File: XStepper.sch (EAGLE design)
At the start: 75 parts, among them IC2 7812TV, Q2 16 MHZ

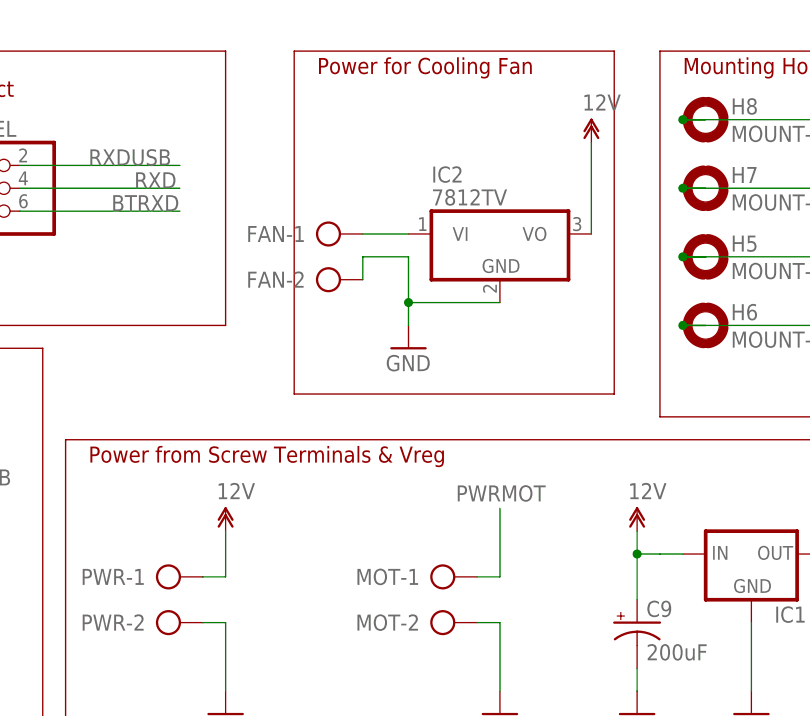
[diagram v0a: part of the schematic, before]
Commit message: - add 7812 regulator for fan and main 5V voltage regulator
- change c10 to small cap cuz he get only 12v with new regulator
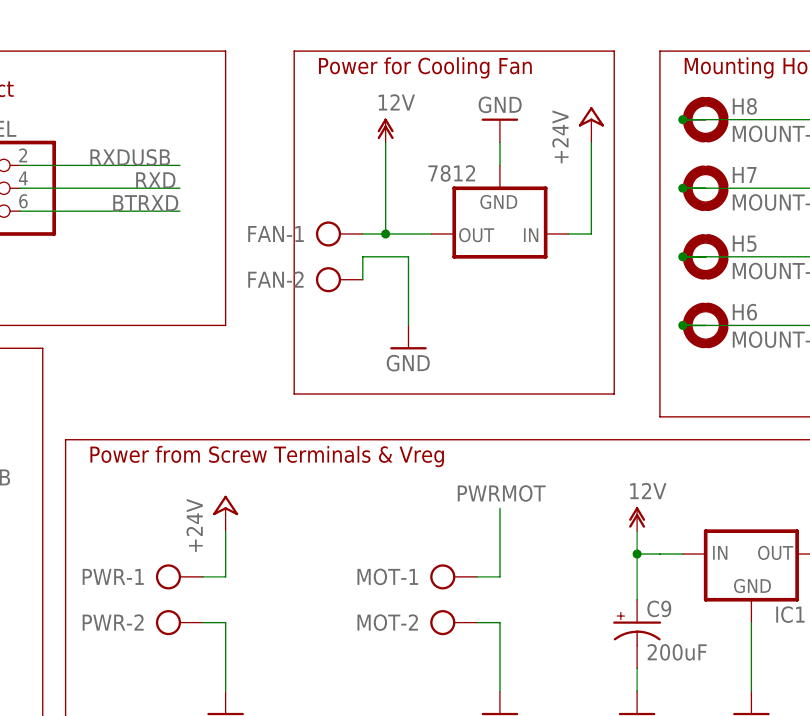
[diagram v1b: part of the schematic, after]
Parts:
- removed IC2: 7812TV, linear:7812TV
- added 7812: (no value), SparkFun-PowerIC:V_REG_78XXSINK
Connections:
- removed net N$46: FAN-1.KL, IC2.VI
- new net +24V: 7812.IN, PWR-1.KL
- net 12V: now also 7812.OUT, FAN-1.KL; no longer IC2.VO, PWR-1.KL
- net GND: now also 7812.GND; no longer IC2.GND
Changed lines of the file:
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@@
 <part name="GND13" library="SparkFun" deviceset="GND" device=""/>
 <part name="GND25" library="SparkFun" deviceset="GND" device=""/>
-<part name="U$33" library="12v" deviceset="12V" device=""/>
 <part name="GND14" library="SparkFun" deviceset="GND" device=""/>
 <part name="GND22" library="SparkFun" deviceset="GND" device=""/>
@@
 <part name="GND21" library="SparkFun" deviceset="GND" device=""/>
 <part name="D2" library="SparkFun-DiscreteSemi" deviceset="DIODE" device="PTH"/>
-<part name="IC2" library="linear" deviceset="78*" device="TV" technology="12"/>
+<part name="7812" library="SparkFun-PowerIC" deviceset="V_REG_78XX" device="SINK"/>
+<part name="GND27" library="SparkFun" deviceset="GND" device=""/>
+<part name="P+1" library="supply1" deviceset="+24V" device=""/>
+<part name="P+2" library="supply1" deviceset="+24V" device=""/>
 <part name="U$2" library="12v" deviceset="12V" device=""/>
 </parts>
@@
 <instance part="GND13" gate="1" x="177.8" y="106.68"/>
 <instance part="GND25" gate="1" x="132.08" y="106.68"/>
-<instance part="U$33" gate="G$1" x="132.08" y="127"/>
 <instance part="GND14" gate="1" x="203.2" y="106.68"/>
 <instance part="GND22" gate="1" x="190.5" y="106.68"/>
@@
 <instance part="GND21" gate="1" x="30.48" y="124.46" rot="R90"/>
 <instance part="D2" gate="G$1" x="236.22" y="165.1"/>
-<instance part="IC2" gate="A1" x="162.56" y="160.02"/>
-<instance part="U$2" gate="G$1" x="172.72" y="170.18"/>
+<instance part="7812" gate="G$1" x="162.56" y="160.02" rot="R180"/>
+<instance part="GND27" gate="1" x="162.56" y="172.72" rot="R180"/>
+<instance part="P+1" gate="1" x="132.08" y="129.54"/>
+<instance part="P+2" gate="1" x="172.72" y="172.72"/>
+<instance part="U$2" gate="G$1" x="149.86" y="170.18"/>
 </instances>
 <busses>
@@
 </segment>
 <segment>
-<wire x1="152.4" y1="149.86" x2="152.4" y2="152.4" width="0.1524" layer="91"/>
 <pinref part="GND18" gate="1" pin="GND"/>
 <pinref part="FAN" gate="-2" pin="KL"/>
-<wire x1="152.4" y1="152.4" x2="152.4" y2="157.48" width="0.1524" layer="91"/>
+<wire x1="152.4" y1="149.86" x2="152.4" y2="157.48" width="0.1524" layer="91"/>
 <wire x1="147.32" y1="154.94" x2="147.32" y2="157.48" width="0.1524" layer="91"/>
 <wire x1="147.32" y1="157.48" x2="152.4" y2="157.48" width="0.1524" layer="91"/>
-<pinref part="IC2" gate="A1" pin="GND"/>
-<wire x1="162.56" y1="152.4" x2="152.4" y2="152.4" width="0.1524" layer="91"/>
-<junction x="152.4" y="152.4"/>
 </segment>
 <segment>
@@
 <wire x1="25.4" y1="124.46" x2="27.94" y2="124.46" width="0.1524" layer="91"/>
 </segment>
+<segment>
+<pinref part="7812" gate="G$1" pin="GND"/>
+<wire x1="162.56" y1="167.64" x2="162.56" y2="170.18" width="0.1524" layer="91"/>
+<pinref part="GND27" gate="1" pin="GND"/>
+</segment>
 </net>
 <net name="N$5" class="0">
@@
 </segment>
 <segment>
-<pinref part="PWR" gate="-1" pin="KL"/>
-<pinref part="U$33" gate="G$1" pin="12V"/>
-<wire x1="129.54" y1="121.92" x2="132.08" y2="121.92" width="0.1524" layer="91"/>
-<wire x1="132.08" y1="121.92" x2="132.08" y2="127" width="0.1524" layer="91"/>
-</segment>
-<segment>
-<pinref part="IC2" gate="A1" pin="VO"/>
-<wire x1="172.72" y1="160.02" x2="172.72" y2="170.18" width="0.1524" layer="91"/>
+<pinref part="7812" gate="G$1" pin="OUT"/>
+<pinref part="FAN" gate="-1" pin="KL"/>
+<wire x1="154.94" y1="160.02" x2="149.86" y2="160.02" width="0.1524" layer="91"/>
 <pinref part="U$2" gate="G$1" pin="12V"/>
+<wire x1="149.86" y1="160.02" x2="147.32" y2="160.02" width="0.1524" layer="91"/>
+<wire x1="149.86" y1="170.18" x2="149.86" y2="160.02" width="0.1524" layer="91"/>
+<junction x="149.86" y="160.02"/>
 </segment>
 </net>
@@
 </segment>
 </net>
-<net name="N$46" class="1">
-<segment>
-<pinref part="FAN" gate="-1" pin="KL"/>
-<pinref part="IC2" gate="A1" pin="VI"/>
-<wire x1="147.32" y1="160.02" x2="152.4" y2="160.02" width="0.1524" layer="91"/>
-</segment>
-</net>
+<net name="+24V" class="1">
+<segment>
+<pinref part="PWR" gate="-1" pin="KL"/>
+<wire x1="129.54" y1="121.92" x2="132.08" y2="121.92" width="0.1524" layer="91"/>
+<wire x1="132.08" y1="121.92" x2="132.08" y2="127" width="0.1524" layer="91"/>
+<pinref part="P+1" gate="1" pin="+24V"/>
+</segment>
+<segment>
+<pinref part="7812" gate="G$1" pin="IN"/>
+<wire x1="170.18" y1="160.02" x2="172.72" y2="160.02" width="0.1524" layer="91"/>
+<wire x1="172.72" y1="160.02" x2="172.72" y2="170.18" width="0.1524" layer="91"/>
+<pinref part="P+2" gate="1" pin="+24V"/>
+</segment>
+</net>

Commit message: - last design from matt
- correct some issues
- run all eagle tests
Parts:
- removed 7812: (no value), SparkFun-PowerIC:V_REG_78XXSINK
- removed ALED, PWRLED1, XLED, XSTLED, YLED, YSTLED, ZLED, ZSTLED: (no value), led:LED3MM
- removed COMMSEL: (no value), pinhead:PINHD-2X3
- removed D2: (no value), SparkFun-DiscreteSemi:DIODEPTH
- removed ESTOP>, MOT: (no value), con-ptr500:AK500/2
- removed GND: (no value), jumper:JP1E
- removed OK1, OK2: 6N137, optocoupler:6N137
- added AD, XD, YD, ZD: green, SparkFun-LED:LED3MM
- added C16: 0.1uF, resistor:C-EU025-025X050
- added C17, C19: 0.1uF, SparkFun-Capacitors:CAP1206
- added C20: 10uF, SparkFun-Capacitors:CAP_POL1206
- added C21: 200uF, resistor:CPOL-USE3.5-8
- added D1: (no value), SparkFun-DiscreteSemi:DIODEPTH
- added DIR: DIR, SparkFun-Passives:SOLDERJUMPER_2WAYW
- added EN: EN, SparkFun-Passives:SOLDERJUMPER_2WAYW
- added ESTOP, VMOT: (no value), con-ptr500:AK500/2
- added IC2: L7812, SparkFun-PowerIC:V_REG_78XXSINK
- added JP2, JP3, JP4: (no value), SparkFun-Connectors:M04PTH
- added JP5, JP6: (no value), SparkFun-Connectors:M03X2POGO_PINS
- added JP7: USBSMD, SparkFun-Connectors:USBSMD
- added JP8: USB-B, SparkFun-Connectors:USBPTH
- added OK3: HCPL2630, optocoupler:HCPL2630
- added R15, R16: 110, SparkFun-Resistors:RESISTORAXIAL-0.3
- added R22, R23: 470, SparkFun-Resistors:RESISTORAXIAL-0.3
- added RX: Grn, SparkFun-LED:LED1206
- added S1: (no value), SparkFun-Electromechanical:TAC_SWITCHSMD
- added SJ4: NO, SparkFun-Passives:SOLDERJUMPERNO
- added TX: Red, SparkFun-LED:LED1206
- added U1: FT232RL-BASICSSOP, SparkFun-DigitalIC:FT232RL-BASICSSOP
- added VCC: orange, SparkFun-LED:LED3MM
- added X, Y, Z: red, SparkFun-LED:LED3MM
- A-AXIS, X-AXIS, Y-AXIS, Z-AXIS: value (none) -> 2x03
- C10: value 100uF -> 47uF
- C9: value 200uF -> 100uF
- IC1: value (none) -> L7805
- JP1: device pinhead:PINHD-2X3 -> SparkFun-Connectors:M04PTH
- R10, R11: value 470 -> 220
- R13, R14: value 220 -> 10K; device SparkFun-Resistors:RESISTORAXIAL-0.3 -> SparkFun-Resistors:RESISTOR1206
- R3: device SparkFun-Resistors:RESISTORPTH-1/6W -> SparkFun-Resistors:RESISTORAXIAL-0.3
- R6, R7: value 110 -> 330
- R8, R9: value 470 -> 1K; device SparkFun-Resistors:RESISTORAXIAL-0.3 -> SparkFun-Resistors:RESISTOR1206
- XLIM, YLIM, ZLIM: device pinhead:PINHD-1X3 -> SparkFun-Connectors:M03POLAR
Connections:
- net MOTOR_DISABLE renamed ENABLE
- removed net +24V: 7812.IN, PWR-1.KL
- removed net 12V: 7812.OUT, C9.+, FAN-1.KL, IC1.IN
- removed net BTRXD: BT-TTL.3, COMMSEL.6
- removed net BTTXD: BT-TTL.4, COMMSEL.5
- removed net N$10: STEPPERDRIVER1.MOT-1A, YMOT-2.KL
- removed net N$27: AMOT-3.KL, STEPPERDRIVER3.MOT-2A
- removed net N$38: R4.1, XLED.A
- removed net N$39: R5.1, YLED.A
- removed net N$40: R6.1, ZLED.A
- removed net N$41: ALED.A, R7.1
- removed net N$42: R13.2, YSTLED.A
- removed net N$44: R14.2, ZSTLED.A
- removed net PWRMOT: C2.+, C4.+, C6.+, C8.+, MOT-1.KL, STEPPERDRIVER.VMOT, STEPPERDRIVER1.VMOT, STEPPERDRIVER2.VMOT, STEPPERDRIVER3.VMOT
- removed net RXD: 328P.PD0(RXD), COMMSEL.4
- removed net RXDUSB: COMMSEL.2, OK2.VO, R9.2
- removed net TXD: 328P.PD1(TXD), COMMSEL.3
- removed net TXDUSB: COMMSEL.1, R11.2
- removed net USB_5V: C11.1, OK1.VCC, OK1.VE, OK2.A, R10.2, TTL.3
- removed net USB_GND: C11.2, GND.1, OK1.GND, TTL.1, TTL.2
- removed net USB_RXD: OK1.VO, R10.1, TTL.5
- removed net USB_TXD: R8.1, TTL.4
- new net +12V: C9.+, FAN-1.KL, IC1.IN, IC2.OUT
- new net 1AA: AMOT-2.KL, JP4.2, STEPPERDRIVER3.MOT-1A
- new net 1AX: JP1.2, STEPPERDRIVER.MOT-1A, XMOT-2.KL
- new net 1AY: JP2.2, STEPPERDRIVER1.MOT-1A, YMOT-2.KL
- new net 1AZ: JP3.2, STEPPERDRIVER2.MOT-1A, ZMOT-2.KL
- new net 1BA: AMOT-1.KL, JP4.1, STEPPERDRIVER3.MOT-1B
- new net 1BX: JP1.1, STEPPERDRIVER.MOT-1B, XMOT-1.KL
- new net 1BY: JP2.1, STEPPERDRIVER1.MOT-1B, YMOT-1.KL
- new net 1BZ: JP3.1, STEPPERDRIVER2.MOT-1B, ZMOT-1.KL
- new net 2AA: AMOT-3.KL, JP4.3, STEPPERDRIVER3.MOT-2A
- new net 2AX: JP1.3, STEPPERDRIVER.MOT-2A, XMOT-3.KL
- new net 2AY: JP2.3, STEPPERDRIVER1.MOT-2A, YMOT-3.KL
- new net 2AZ: JP3.3, STEPPERDRIVER2.MOT-2A, ZMOT-3.KL
- new net 2BA: AMOT-4.KL, JP4.4, STEPPERDRIVER3.MOT-2B
- new net 2BX: JP1.4, STEPPERDRIVER.MOT-2B, XMOT-4.KL
- new net 2BY: JP2.4, STEPPERDRIVER1.MOT-2B, YMOT-4.KL
- new net 2BZ: JP3.4, STEPPERDRIVER2.MOT-2B, ZMOT-4.KL
- new net BT_RXD: BT-TTL.4, JP5.6
- new net BT_TXD: BT-TTL.3, JP5.5
- new net DTR: C13.1, R13.2, TTL.6
- new net FTDI_RX: JP6.6, U1.RXD
- new net FTDI_TX: JP6.5, R14.2
- new net N$46: OK3B.C2, R23.2
- new net N$47: OK3A.C1, R22.2
- new net OPTO_RX: JP6.4, OK3B.VO2, R7.1
- new net OPTO_TX: JP6.3, R22.1
- new net RX: 328P.PD0(RXD), JP5.3
- new net RXD_USB: JP5.2, R23.1
- new net TTL/USB_5V: C19.1, C20.+, JP7.VBUS, JP8.VBUS, OK3A.A1, R7.2, TTL.3, U1.VCC, U1.VCCIO
- new net TTL_RX: JP6.2, TTL.5
- new net TTL_TX: JP6.1, TTL.4
- new net TX: 328P.PD1(TXD), JP5.4
- new net TXD_USB: JP5.1, OK3A.VO1, R6.1
- new net VIN: C21.+, IC2.IN, PWR-1.KL
- new net VMOT: C2.+, C4.+, C6.+, C8.+, STEPPERDRIVER.VMOT, STEPPERDRIVER1.VMOT, STEPPERDRIVER2.VMOT, STEPPERDRIVER3.VMOT, VMOT-1.KL
- net 5V: now also C1.1, C11.2, C16.2, C3.1, C5.1, C7.1, D1.A, OK3A.VCC, OK3B.A2, R3.2, R6.2, R8.2, R9.2, X.A, XLIM.3, Y.A, YLIM.3, Z.A, ZLIM.3; no longer C1.2, C3.2, C5.2, C7.2, D2.A, OK1.A, OK2.VCC, OK2.VE, R3.1, R9.1, XLIM.1, YLIM.1, ZLIM.1
- net A-DIR: now also DIR.2; no longer JP1.4
- net A-STEP: now also AD.A, EN.2; no longer JP1.3, R7.2
- net GND: now also C1.2, C11.1, C16.1, C17.2, C19.2, C20.-, C21.-, C3.2, C5.2, C7.2, ESTOP-2.KL, IC2.GND, JP7.GND, JP8.GND, OK3A.GND, R15.2, R16.2, R4.2, R5.2, S1.1, S1.2, SJ4.2, TTL.1, U1.AGND, U1.GND1, U1.GND2, U1.GND3, U1.TEST, VCC.C, VMOT-2.KL, XLIM.2, YLIM.2, ZLIM.2; no longer 7812.GND, ALED.C, C1.1, C13.1, C3.1, C5.1, C7.1, ESTOP>-2.KL, GND.2, MOT-2.KL, OK2.GND, PWRLED1.C, XLED.C, XLIM.3, XSTLED.C, YLED.C, YLIM.3, YSTLED.C, ZLED.C, ZLIM.3, ZSTLED.C
- net N$1: now also C17.1, U1.3V3OUT; no longer STEPPERDRIVER.MOT-1B, XMOT-1.KL
- net N$11: now also TX.C, U1.TXLED; no longer STEPPERDRIVER1.MOT-2A, YMOT-3.KL
- net N$12: now also RX.C, U1.RXLED; no longer STEPPERDRIVER1.MOT-2B, YMOT-4.KL
- net N$17: now also R9.1, RX.A; no longer STEPPERDRIVER2.MOT-2B, ZMOT-4.KL
- net N$18: now also R8.1, TX.A; no longer STEPPERDRIVER2.MOT-2A, ZMOT-3.KL
- net N$19: now also SJ4.1, U1.CTS; no longer STEPPERDRIVER2.MOT-1A, ZMOT-2.KL
- net N$2: now also JP7.D+, JP8.D+, U1.USBDP; no longer STEPPERDRIVER.MOT-1A, XMOT-2.KL
- net N$20: now also R4.1, XD.C; no longer STEPPERDRIVER2.MOT-1B, ZMOT-1.KL
- net N$25: now also R5.1, YD.C; no longer AMOT-1.KL, STEPPERDRIVER3.MOT-1B
- net N$26: now also R15.1, ZD.C; no longer AMOT-2.KL, STEPPERDRIVER3.MOT-1A
- net N$28: now also AD.C, R16.1; no longer AMOT-4.KL, STEPPERDRIVER3.MOT-2B
- net N$3: now also JP7.D-, JP8.D-, U1.USBDM; no longer STEPPERDRIVER.MOT-2A, XMOT-3.KL
- net N$35: now also R10.2, X.C; no longer OK2.C, R8.2
- net N$36: now also R11.2, Y.C; no longer OK1.C, R11.1
- net N$37: now also Z.C; no longer XSTLED.A
- net N$4: now also R13.1, U1.DTR; no longer STEPPERDRIVER.MOT-2B, XMOT-4.KL
- net N$43: now also R3.1, VCC.A; no longer PWRLED1.A, R3.2
- net N$45: now also D1.C; no longer D2.C
- net N$9: now also R14.1, U1.TXD; no longer STEPPERDRIVER1.MOT-1B, YMOT-1.KL
- net RESET: now also ESTOP-1.KL, S1.3, S1.4; no longer ESTOP>-1.KL
- net SPINDLE-DIR: now also DIR.3; no longer JP1.2
- net SPINDLE-ENABLE: now also EN.1; no longer JP1.1
- net X-STEP: now also XD.A; no longer R4.2
- net X-STOP: now also R10.1, XLIM.1; no longer R12.1, XLIM.2
- net Y-DIR: now also DIR.1; no longer JP1.6
- net Y-STEP: now also EN.3, YD.A; no longer JP1.5, R5.2
- net Y-STOP: now also R11.1, YLIM.1; no longer R13.1, YLIM.2
- net Z-STEP: now also ZD.A; no longer R6.2
- net Z-STOP: now also R12.1, ZLIM.1; no longer R14.1, ZLIM.2
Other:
- note added: "Cooling Fan"
- note added: "ENDSTOPS"
- note added: "FTDI"
- note added: "Motor Power"
- note added: "Mounting Holes"
- note removed: "Mounting Holes to gnd"
- note removed: "Power LED"
- note removed: "Power for Cooling Fan"
- note removed: "XBEE-EXTENSION"
- moved on the sheet: 328P, A-AXIS, AMOT-1, AMOT-2, AMOT-3, AMOT-4, BT-TTL, C1, C10, C11, C12, C13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

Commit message: - some changes from matt and produce in fab 0.95
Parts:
- removed C14, C15: 18pF, resistor:C-EU025-025X050
- removed C9: 100uF, resistor:CPOL-USE2.5-6
- removed R11: 220, SparkFun-Resistors:RESISTORAXIAL-0.3
- removed R3: 330, SparkFun-Resistors:RESISTORAXIAL-0.3
- removed R5: 110, SparkFun-Resistors:RESISTORAXIAL-0.3
- added C22, C30: 0.1uF, resistor:C-EU025-025X050
- added C32: 10uF, SparkFun-Capacitors:CAP_POL1206
- added JP9: (no value), SparkFun-Connectors:M02PTH
- added R21: 330, SparkFun-Resistors:RESISTORAXIAL-0.3
- added R30, R31: 470, SparkFun-Resistors:RESISTORAXIAL-0.3
- added SJ1: NO, SparkFun-Passives:SOLDERJUMPERNO
- A-AXIS, X-AXIS, Y-AXIS, Z-AXIS: value 2x03 -> (none)
- AD, XD, YD, ZD: value green -> Gr
- C1: value 0.1uF -> 18pF
- C10: value 47uF -> 200uF; device resistor:CPOL-USE2.5-6 -> resistor:CPOL-USE3.5-8
- C11: value 0.1uF -> 100uF; device resistor:C-EU025-025X050 -> resistor:CPOL-USE2.5-6
- C12: value 0.1uF -> 47uF; device resistor:C-EU025-025X050 -> resistor:CPOL-USE2.5-6
- C2: value 100uF -> 18pF; device resistor:CPOL-USE3.5-8 -> resistor:C-EU025-025X050
- C20: value 10uF -> 0.1uF; device SparkFun-Capacitors:CAP_POL1206 -> resistor:C-EU025-025X050
- C21: value 200uF -> 100uF
- R10, R25: value 220 -> 330
- R22: value 470 -> 110
- R23: value 470 -> 330
- VCC: value orange -> Or
- X, Y, Z: value red -> Rd
- renumbered C16 to C31, C17 to C34, C19 to C33, C4 to C23, C5 to C24, C6 to C25, C7 to C26, C8 to C27, R12 to R25, R13 to R35, R14 to R34, R15 to R24, R16 to R26, R4 to R20, R6 to R32, R7 to R33, R8 to R36, R9 to R37
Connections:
- new net N$10: SJ1.1, TTL.2
- new net USB_GND: C32.-, C33.2, C34.2, JP7.GND, JP8.GND, JP9.1, SJ1.2, SJ4.2, TTL.1, U1.AGND, U1.GND1, U1.GND2, U1.GND3, U1.TEST
- net +12V: now also C11.+; no longer C9.+
- net 5V: now also C12.+, C13.2, C20.1, C22.1, C3.2, R10.2; no longer C1.1, C10.+, C11.2, C12.2, C3.1, R3.2
- net DTR: now also C30.1; no longer C13.1
- net GND: now also C11.-, C12.-, C13.1, C2.2, C20.2, C22.2, C3.1, JP9.2, R22.2; no longer C11.1, C12.1, C14.2, C15.2, C2.-, C20.-, C3.2, C33.2, C34.2, C9.-, JP7.GND, JP8.GND, R5.2, SJ4.2, TTL.1, U1.AGND, U1.GND1, U1.GND2, U1.GND3, U1.TEST
- net N$25: now also R22.1; no longer R5.1
- net N$33: now also C1.1; no longer C15.1
- net N$34: now also C2.1; no longer C14.1
- net N$35: now also R21.2; no longer R10.2
- net N$36: now also R23.2; no longer R11.2
- net N$43: now also R10.1; no longer R3.1
- net N$46: now also R31.2; no longer R23.2
- net N$47: now also R30.2; no longer R22.2
- net OPTO_TX: now also R30.1; no longer R22.1
- net RESET: now also C30.2; no longer C13.2
- net RXD_USB: now also R31.1; no longer R23.1
- net TTL/USB_5V: now also C32.+; no longer C20.+
- net VIN: now also C10.+; no longer C21.+
- net VMOT: now also C21.+; no longer C2.+
- net X-STOP: now also R21.1; no longer R10.1
- net Y-STOP: now also R23.1; no longer R11.1
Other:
- moved on the sheet: C1, C10, C13, C21, C3, R10, R22, R23, TTL

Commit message: - gerber files for ITEAD 0.96
- new pic for docs
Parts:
- JP5, JP6: device SparkFun-Connectors:M03X2POGO_PINS -> pinhead:PINHD-2X3
- JP9: value (none) -> M02PTH
- renumbered EN to STEP, S1 to S2
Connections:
- net 5V: no longer R36.2, R37.2
- net TTL/USB_5V: now also R36.2, R37.2
